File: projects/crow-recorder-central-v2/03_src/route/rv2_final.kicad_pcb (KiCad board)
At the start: 6 copper layers, 170 x 120 mm, 198 parts, among them J1 C381116, J10 C9900035627, J2 C3020560, J3 C9900035627, J4 C9900035627, J5 C9900035627, J6 C9900035627, J7 C9900035627, J8 C9900035627, J9 C9900035627, Q1 C15127, Q2 C20917, U1 C6938291, U10 C6035451, U2 C181312, U3 C181312, U4 C232798, U5 C82317, U6 C2909890, U7 C5224055, U8 C5224055, U9 C150173, Y1 C7190380

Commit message: crow-recorder-central-v2 WIP checkpoint: mid-P0 fix pass at the 2026-07-23 quota stop
Session-quota interruption checkpoint. Carries the interrupted P5VA_4
net-merge surgery (schematic doglegs, merged-net tree deletion, port-4 +
channel-2 re-route, 5V island reconnection), check_port_nets.py (the
label-survival gate that found the SECOND merge MID2P->5V the red-team
missed), ADR-0007 PoE-backfeed draft, rebuild_reuse.sh driver, BLM21
part. NOT a green gate — DRC re-verify + scoped re-red-team still owed
(RESUME.md is the brief). GUARD from the red-team dispositions: Q1
reverse-polarity is CORRECT as-built (rejected finding — do not "fix").

Co-Authored-By: Claude Fable 5 <noreply@anthropic.com>
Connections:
- Cc2P pad 2: 5V -> MID2P
- F4 pad 2: AUDIO4M -> P5VA_4
- J6 pad 4: AUDIO4M -> P5VA_4
- J6 pad 7: AUDIO4M -> P5VA_4
- Rs2P pad 1: 5V -> MID2P
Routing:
- net P5VA_4: track 0.00 -> 24.2 mm, vias 0 -> 2
- net MID2P: track 0.00 -> 13.3 mm, vias 0 -> 2
- net 5V: track 371.4 -> 358.7 mm
- net AUDIO4M: track 74.8 -> 63.6 mm, vias 0 -> 2

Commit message: crow-central v1.1: F1+F2 implemented, routing gate GREEN 0/0/0 from committed source
F1 (U1 EP via-in-pad): footprint thru-pads removed; rebuild step 3.5 seeds
16 REAL GND 0.30/0.15 vias on the 4x4 EP grid; step 4.5 sets board setup
(capping yes)(filling yes). MEASURED: PTH drill now emits NO 0.15
ComponentDrill tool at all — T1 ViaDrill 0.150 carries all 639 vias incl.
the 16 EP holes at (90,102)+/-{0.55,1.65}; remaining ComponentDrill tools
are real THT (0.6/0.89/1.0/1.57). audit_board gains the U1-EP 16-GND-via
gate.

F2 (USB HS 90ohm): promoted converter sch guarded in rebuild_all (the P0
dogleg surgery is a promoted artifact — a fresh converter render measurably
reintroduces the P5VA_4/MID2P merge class, check_port_nets RED); USB_DM ->
USB_DN rename (KiCad pairs only P/N suffixes); USB_DIFF netclass
diff_pair {w 0.125, gap 0.15} solved for JLC06161H-3313 (2D FD field
solve 89.7-90.5 ohm, sanity 50.6 ohm SE at w0.14); KRT route_diff reroute:
pair coupled at 0.155mm centers-gap measured, all F.Cu, 0 vias, lengths
DP 23.62 / DN 23.51, spread 0.110mm <= 1mm; chain re-promoted.
ACTIVATION PROOF (a gate that cannot fail is worthless): tightening the
dru min to 0.30mm produced 10 diff_pair_gap_out_of_range violations on a
board copy — the rule fires on this exact pair; restored rule re-gates
0/0/0. check_port_nets 115/115 + 8/8 re-verified after reroute.

Co-Authored-By: Claude Fable 5 <noreply@anthropic.com>
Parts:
- CL1, CL2: value 22pF -> 12pF
- Cout_U10: value 1uF -> 2.2uF
- R_fb2b: value 400kΩ -> 402kΩ
- U9: value C150173 -> C79924
- Y1: value C7190380 -> C2762192
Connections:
- net USB_DM renamed USB_DN
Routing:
- net USB_DN: track 24.2 -> 23.6 mm
- net USB_DP: track 23.5 -> 23.7 mm, vias 2 -> 0
- added copper zone on F.Cu, net 5V
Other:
- board text added: "NOT ETH 5V!"

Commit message: crow-central v1.1: LV straps floated (PR2-P0-1 fix) + re-gate green, pre-lens checkpoint
U1.40/43/52 3V3 tie removed at source (tsx + promoted-sch surgery: 14
wires + 1 label excised — BFS-proven self-contained branch — + 3
no_connect markers = the ds v2.0.0 sec 4.8 float select); chain surgery
removed exactly 7 copper items (3 in-pad 3V3 vias + 4 dead segments; a
first graph-prune attempt over-deleted 9 zone/T-anchored segments and was
reverted from git before redoing as an explicit list). part.yaml strap
facts corrected (HIGH = IOB 1.8V, never 3V3).

Re-gate MEASURED: DRC 0/0/0 (+ staged-archive standalone 0/0/0); parity 0
(588 nodes / 146 no-connects both sides); ERC 0 err / 1201 warn (-14 =
excised branch); check_port_nets 115/115 + 8/8; audit_board green (USB
spread 0.110mm, U1-EP 16 GND vias); twin exit 0 (160 OK/359); BOM source
PASS vs the staged dir; v1.0-relative netlist diff = EXACTLY 7 node moves
(4x USB_DM->USB_DN + 3x LV to unconnected) — 06_build/verify/
lv_strap_fix_diff.md. Pin + render reviews archived verbatim in
08_reviews/ (both PASS; pin review's LV finding escalated, datasheet-
confirmed, fixed). Staged v1.1 dir refreshed to the fixed bytes; MANIFEST
still unstamped (seal step 2 pending fresh lens).

Co-Authored-By: Claude Fable 5 <noreply@anthropic.com>
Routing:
- net 3V3: track 364.8 -> 359.9 mm, vias 29 -> 26

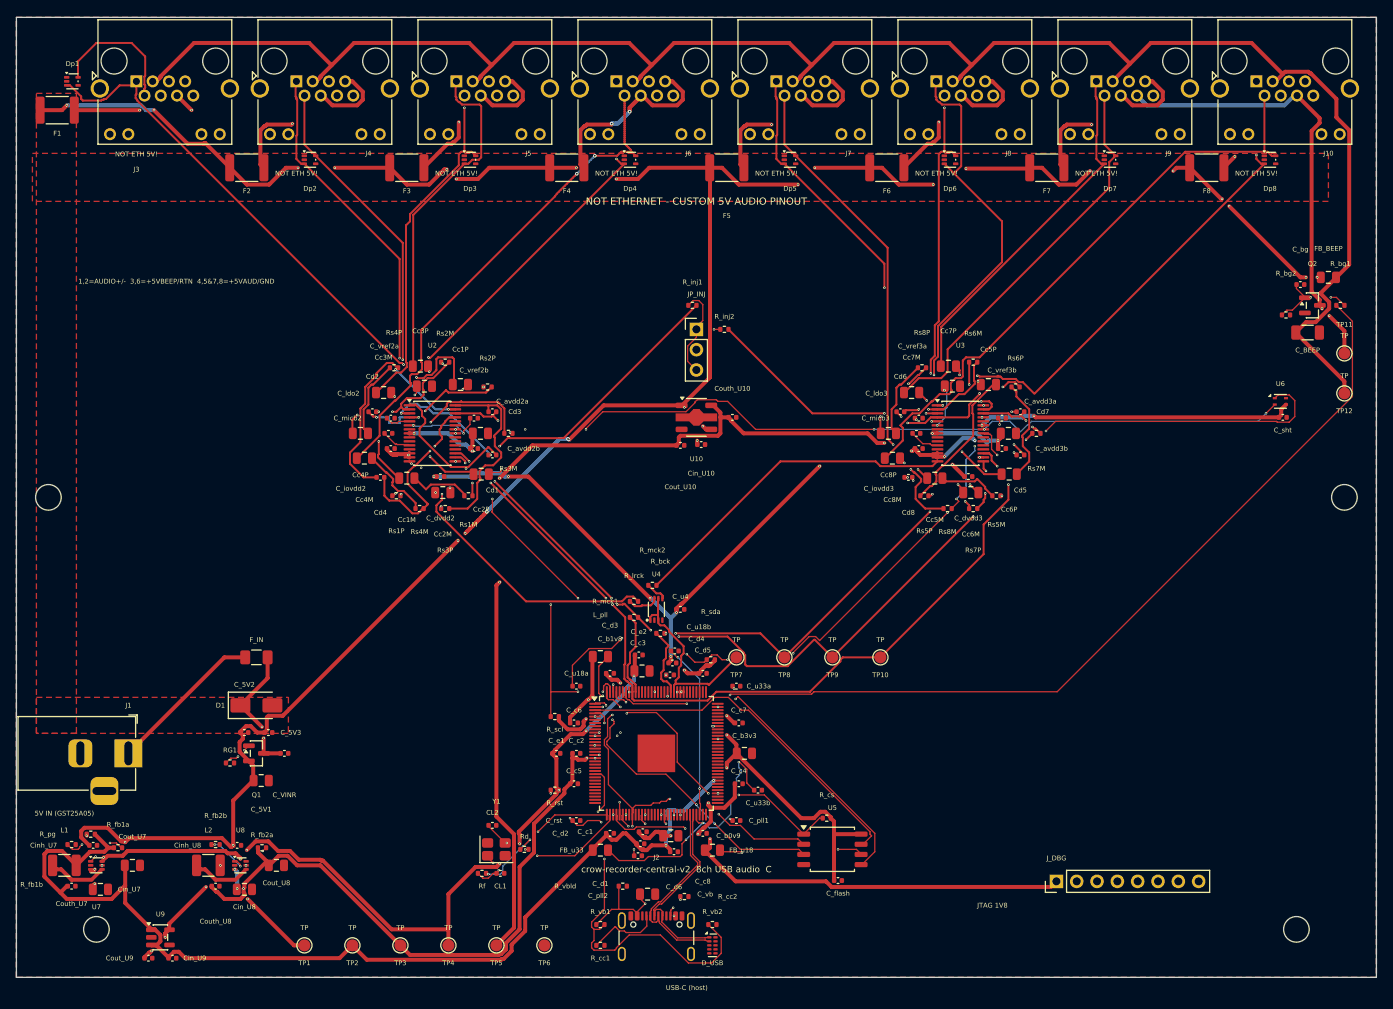
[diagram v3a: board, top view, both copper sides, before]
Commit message: crow-central v1.2: XU316 core decoupling to vendor minimum — 13x 100nF on 0V9, routing gate GREEN
Driver: 2nd external v1.1 review (EXT2-F1, archived verbatim in 08_reviews
with provenance + orchestrator verification): 8x 100nF on the 0V9 core rail
for 15 core-VDD pins vs the vendor minimum. Vendor number VERIFIED at the
source, not taken from the reviewer: XU316-1024-TQ128 ds XM-014532-PC-2.0.0
§14 'Integration' p.29 — 'Place many (at least 12) 100 nF low inductance
multi-layer ceramic capacitors close to the chip' (§H.2 p.92 agrees).

The fix (all at source, canon M3):
- tsx 8->13 C_c caps; manifest +5; promoted-sch IN-PLACE surgery (LV-strap
  precedent — regeneration drops the P5VA_4/MID2P doglegs): measured netlist
  diff vs v1.1 = EXACTLY {C_c9..C_c13} x {0V9,GND}.
- Placement: 5 anchors at scan-verified spots hard against the under-served
  pins; the 32 U1-cluster floaters PINNED at their v1.1 positions (the new
  anchors changed the legalizer walk and moved all 32 — measured — which
  would have invalidated the whole promoted chain).
- C_b0v9 slot swap: U1 courtyard vs the C_c1/C_b0v9 row leaves no 0402 slot
  at pins 50/54; the 10uF bulk (no pin-adjacency requirement, ds §14) moved
  3.75mm south; C_c11/C_c13 take its slot at 2.01/2.02mm from pins 50/54.
- Chain surgery: TDI F.Cu run -> In3 (frees the south band); 0V9 feeder
  rerouted at 0.4; 4x 0.30mm taps into pads 14/50/54/95 with scoped floors
  (0.4 into a 0.4mm-pitch row violates neighbor clearance by construction);
  C_b0v9 B.Cu feed with 2 vias; title caption relocated.
- C_c11 pad2 starved_thermal -> pad_overrides FULL (golden rule 9).

Gate: rebuild_reuse.sh from committed source = DRC 0/0/0 (severity-all +
refill + schematic-parity); port nets 115/115 + 8/8. Survival measured:
USB pair 23.621/23.511mm skew 0.110mm all-0.125 F.Cu 0 vias; U1 EP 16x
0.3/0.15 GND vias; LV straps 40/43/52 unconnected. Worst pin-to-nearest-cap
3.22mm. Per-pin map in journal/routing.md.

Co-Authored-By: Claude Opus 5 <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
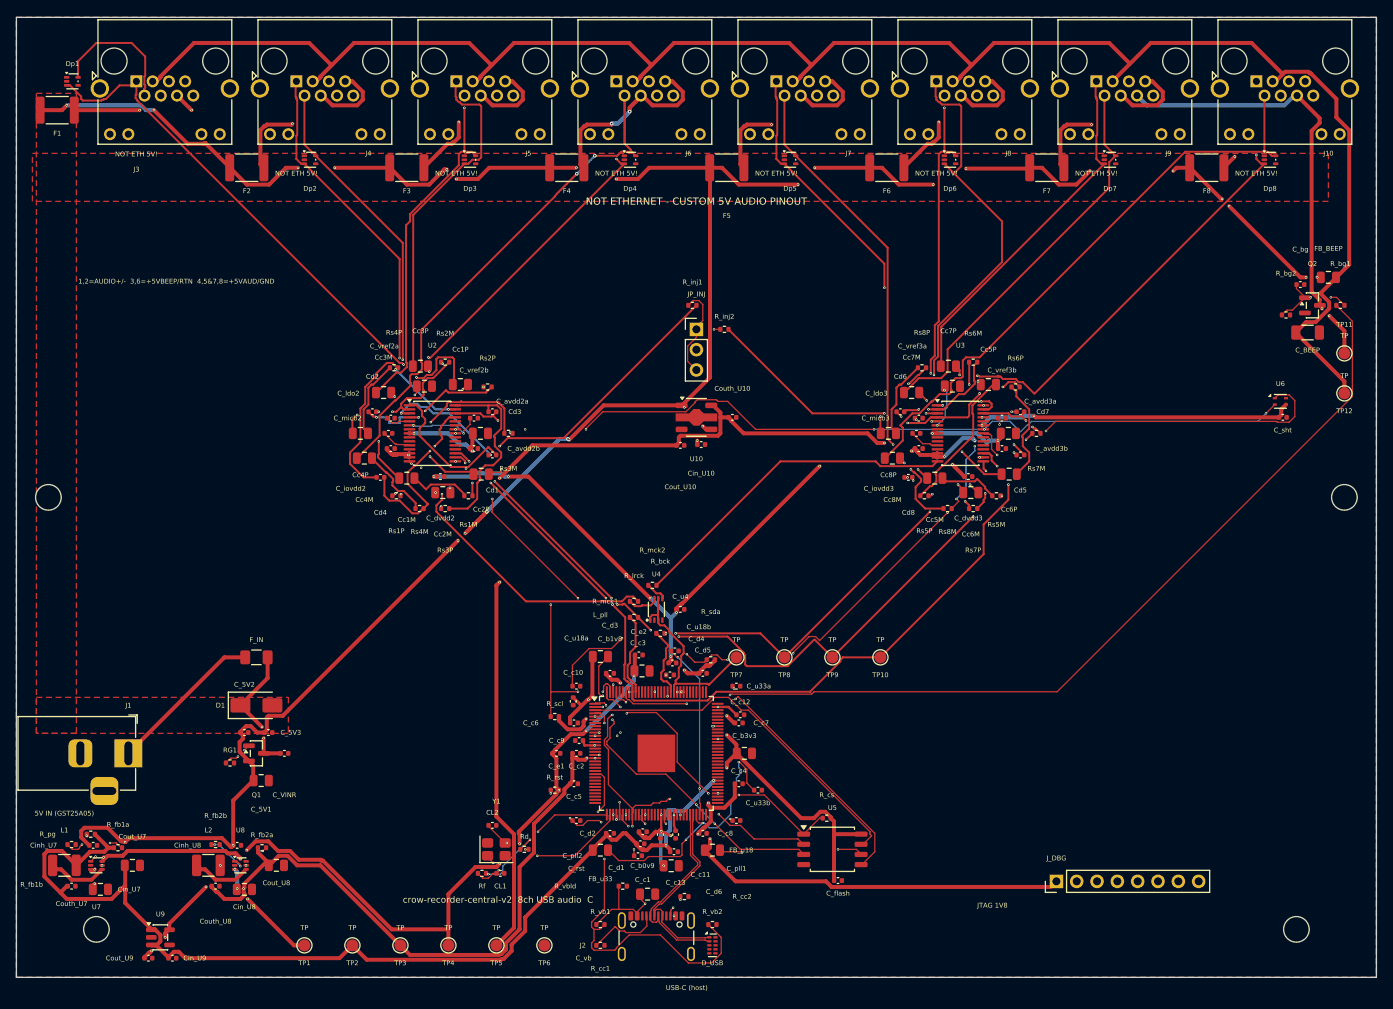
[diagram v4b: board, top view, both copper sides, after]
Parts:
- added C_c10: 100nF, Capacitor_SMD:C_0402_1005Metric, F.Cu at (79.6, 95.5)
- added C_c11: 100nF, Capacitor_SMD:C_0402_1005Metric, F.Cu at (90.5, 112.2)
- added C_c12: 100nF, Capacitor_SMD:C_0402_1005Metric, F.Cu at (100.5, 97.2)
- added C_c13: 100nF, Capacitor_SMD:C_0402_1005Metric, F.Cu at (92.4, 112.2)
- added C_c9: 100nF, Capacitor_SMD:C_0402_1005Metric, F.Cu at (80.3, 100.4)
- moved C_b0v9 3.75 mm to (91.8, 116.0)
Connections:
- U1 pad 40: 3V3 -> unconnected-(U1-Pad40)
- U1 pad 43: 3V3 -> unconnected-(U1-Pad43)
- U1 pad 52: 3V3 -> unconnected-(U1-Pad52)
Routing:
- net 0V9: track 167.1 -> 181.4 mm, vias 23 -> 25
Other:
- board text added: "C_c10"
- board text added: "C_c11"
- board text added: "C_c12"
- board text added: "C_c13"
- board text added: "C_c9"
